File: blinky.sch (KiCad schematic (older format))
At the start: 38 parts, among them J1 MIC_CLK, J10 DEBUG, J11 SWD, J12 BATTERY, J13 UART, J14 5V, J15 3V3, J2 MIC_DOUT, J3 LED_DIN, J4 ACCEL_MISO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

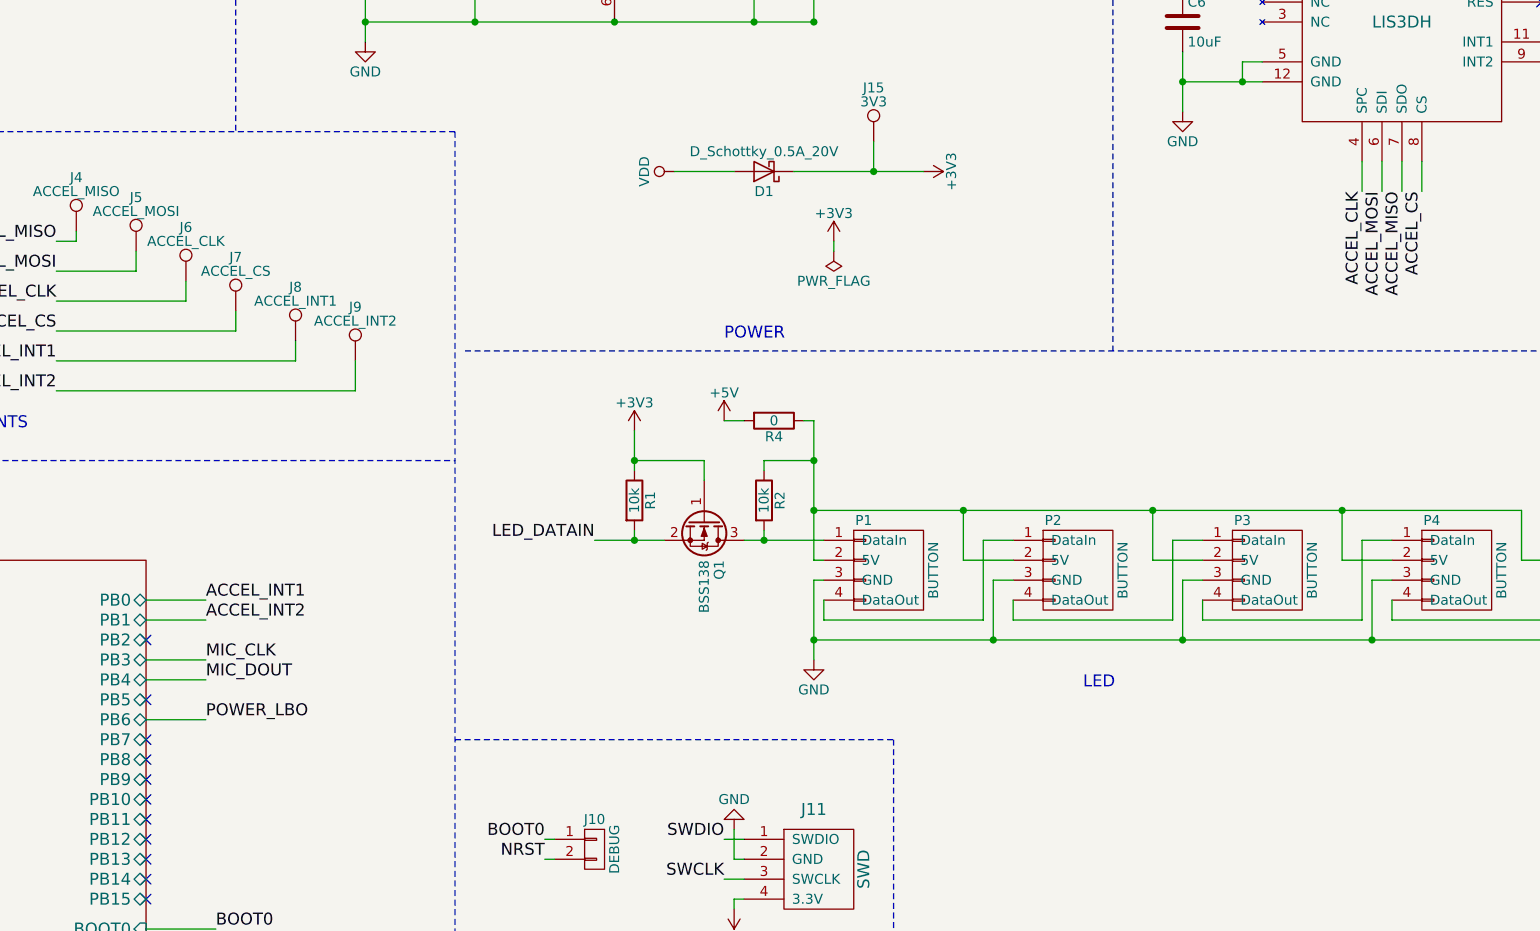
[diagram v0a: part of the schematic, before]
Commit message: Add heartbeat led
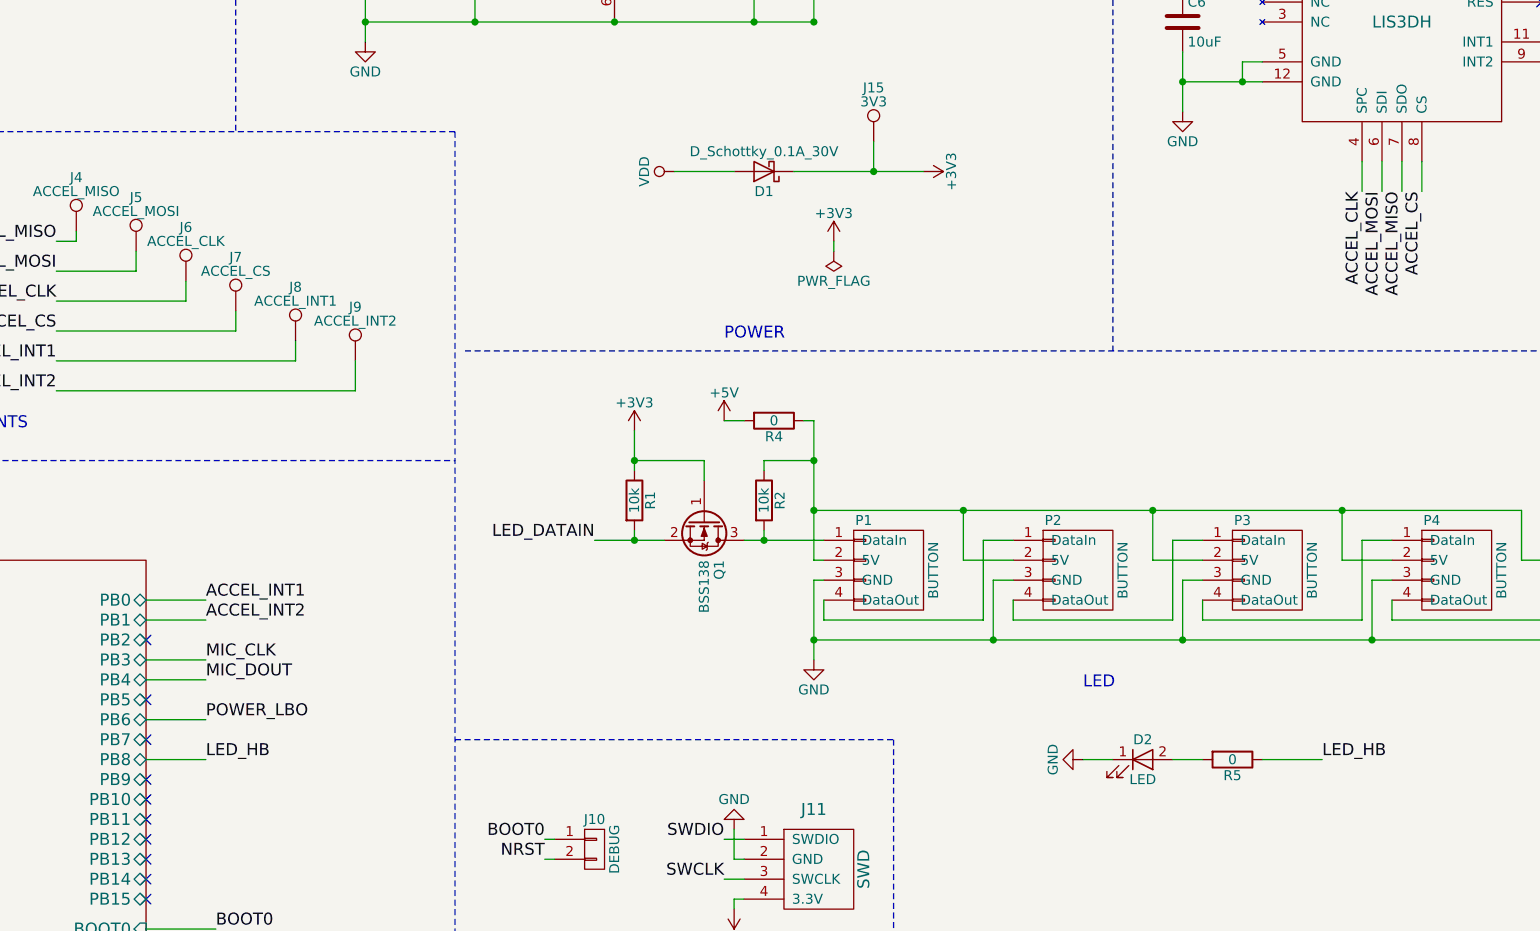
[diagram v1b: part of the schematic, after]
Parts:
- added D2: LED, Diodes_SMD:D_0603, symbol LED
- added R5: 0, Resistors_SMD:R_0603, symbol R
- D1: value D_Schottky_0.5A_20V -> D_Schottky_0.1A_30V; footprint Diodes_SMD:SOD-523 -> Diodes_SMD:D_0603; MFR Nexperia -> Comchip Technology; MPN PMEG2005EB,115 -> CDBU0130L; PN PMEG2005EB,115 -> (none); SPN 771-PMEG2005EBT/R -> 750-CDBU0130L
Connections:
- net GND: now also D2.1 (K)
- new net: D2.2 (A), R5.2
- new net LED_HB: R5.1
- no-connect marks 24 -> 23
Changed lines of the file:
@@
 EESchema Schematic File Version 2
-LIBS:blinky-rescue
 LIBS:power
 LIBS:device
@@
 $EndSheet
 $Comp
-L GND #PWR01
+L GND #PWR19
 U 1 1 59735157
 P 8250 2650
-F 0 "#PWR01" H 8250 2400 50  0001 C CNN
+F 0 "#PWR19" H 8250 2400 50  0001 C CNN
 F 1 "GND" H 8250 2500 50  0000 C CNN
 F 2 "" H 8250 2650 50  0001 C CNN
@@
 $EndComp
 $Comp
-L GND #PWR02
+L GND #PWR21
 U 1 1 59735414
 P 8450 1250
-F 0 "#PWR02" H 8450 1000 50  0001 C CNN
+F 0 "#PWR21" H 8450 1000 50  0001 C CNN
 F 1 "GND" H 8450 1100 50  0000 C CNN
 F 2 "" H 8450 1250 50  0001 C CNN
@@
 $EndComp
 $Comp
-L +5V #PWR03
+L +5V #PWR8
 U 1 1 59735989
 P 5950 4200
-F 0 "#PWR03" H 5950 4050 50  0001 C CNN
+F 0 "#PWR8" H 5950 4050 50  0001 C CNN
 F 1 "+5V" H 5950 4340 50  0000 C CNN
 F 2 "" H 5950 4200 50  0001 C CNN
@@
 $EndComp
 $Comp
-L GND #PWR04
+L GND #PWR13
 U 1 1 597359AA
 P 6400 5400
-F 0 "#PWR04" H 6400 5150 50  0001 C CNN
+F 0 "#PWR13" H 6400 5150 50  0001 C CNN
 F 1 "GND" H 6400 5250 50  0000 C CNN
 F 2 "" H 6400 5400 50  0001 C CNN
@@
 $EndComp
 $Comp
-L GND #PWR05
+L GND #PWR9
 U 1 1 59736818
 P 6000 6250
-F 0 "#PWR05" H 6000 6000 50  0001 C CNN
+F 0 "#PWR9" H 6000 6000 50  0001 C CNN
 F 1 "GND" H 6000 6100 50  0000 C CNN
 F 2 "" H 6000 6250 50  0001 C CNN
@@
 $EndComp
 $Comp
-L VDD #PWR06
+L VDD #PWR3
 U 1 1 5974FA3E
 P 4150 1000
-F 0 "#PWR06" H 4150 850 50  0001 C CNN
+F 0 "#PWR3" H 4150 850 50  0001 C CNN
 F 1 "VDD" H 4150 1150 50  0000 C CNN
 F 2 "" H 4150 1000 50  0001 C CNN
@@
 $EndComp
 $Comp
-L GND #PWR07
+L GND #PWR4
 U 1 1 5974FA44
 P 4150 2300
-F 0 "#PWR07" H 4150 2050 50  0001 C CNN
+F 0 "#PWR4" H 4150 2050 50  0001 C CNN
 F 1 "GND" H 4150 2150 50  0000 C CNN
 F 2 "" H 4150 2300 50  0001 C CNN
@@
 $EndComp
 $Comp
-L +5V #PWR08
+L +5V #PWR15
 U 1 1 5974FA78
 P 6750 1000
-F 0 "#PWR08" H 6750 850 50  0001 C CNN
+F 0 "#PWR15" H 6750 850 50  0001 C CNN
 F 1 "+5V" H 6750 1140 50  0000 C CNN
 F 2 "" H 6750 1000 50  0001 C CNN
@@
 $EndComp
 $Comp
-L +3V3 #PWR09
+L +3V3 #PWR16
 U 1 1 5974FA92
 P 6950 2950
-F 0 "#PWR09" H 6950 2800 50  0001 C CNN
+F 0 "#PWR16" H 6950 2800 50  0001 C CNN
 F 1 "+3V3" H 6950 3090 50  0000 C CNN
 F 2 "" H 6950 2950 50  0001 C CNN
@@
 P 6150 2950
 F 0 "D1" H 6150 3050 50  0000 C CNN
-F 1 "D_Schottky_0.5A_20V" H 6150 2850 50  0000 C CNN
-F 2 "Diodes_SMD:SOD-523" H 6150 2950 50  0001 C CNN
+F 1 "D_Schottky_0.1A_30V" H 6150 2850 50  0000 C CNN
+F 2 "Diodes_SMD:D_0603" H 6150 2950 50  0001 C CNN
 F 3 "" H 6150 2950 50  0001 C CNN
-F 4 "PMEG2005EB,115" H 6150 2950 60  0001 C CNN "PN"
-F 5 "Nexperia" H -1200 1750 50  0001 C CNN "MFR"
-F 6 "PMEG2005EB,115" H -1200 1750 50  0001 C CNN "MPN"
-F 7 "Mouser" H -1200 1750 50  0001 C CNN "SPR"
-F 8 "771-PMEG2005EBT/R" H -1200 1750 50  0001 C CNN "SPN"
-F 9 "" H -1200 1750 50  0001 C CNN "SPURL"
+F 4 "Comchip Technology" H -1200 1750 50  0001 C CNN "MFR"
+F 5 "CDBU0130L" H -1200 1750 50  0001 C CNN "MPN"
+F 6 "Mouser" H -1200 1750 50  0001 C CNN "SPR"
+F 7 "750-CDBU0130L" H -1200 1750 50  0001 C CNN "SPN"
 	1    6150 2950
 	-1   0    0    1
 $EndComp
 $Comp
-L +3V3 #PWR010
+L +3V3 #PWR18
 U 1 1 5974FC09
 P 8250 1900
-F 0 "#PWR010" H 8250 1750 50  0001 C CNN
+F 0 "#PWR18" H 8250 1750 50  0001 C CNN
 F 1 "+3V3" H 8250 2040 50  0000 C CNN
 F 2 "" H 8250 1900 50  0001 C CNN
@@
 $EndComp
 $Comp
-L +3V3 #PWR011
+L +3V3 #PWR20
 U 1 1 5974FD08
 P 8450 800
-F 0 "#PWR011" H 8450 650 50  0001 C CNN
+F 0 "#PWR20" H 8450 650 50  0001 C CNN
 F 1 "+3V3" H 8450 940 50  0000 C CNN
 F 2 "" H 8450 800 50  0001 C CNN
@@
 $EndComp
 $Comp
-L +3V3 #PWR012
+L +3V3 #PWR6
 U 1 1 5974FDE2
 P 5500 4250
-F 0 "#PWR012" H 5500 4100 50  0001 C CNN
+F 0 "#PWR6" H 5500 4100 50  0001 C CNN
 F 1 "+3V3" H 5500 4390 50  0000 C CNN
 F 2 "" H 5500 4250 50  0001 C CNN
@@
 $EndComp
 $Comp
-L +3V3 #PWR013
+L +3V3 #PWR10
 U 1 1 5974FF6A
 P 6000 6650
-F 0 "#PWR013" H 6000 6500 50  0001 C CNN
+F 0 "#PWR10" H 6000 6500 50  0001 C CNN
 F 1 "+3V3" H 6000 6790 50  0000 C CNN
 F 2 "" H 6000 6650 50  0001 C CNN
@@
 $EndComp
 $Comp
-L +3V3 #PWR014
+L +3V3 #PWR1
 U 1 1 59757575
 P 800 1150
-F 0 "#PWR014" H 800 1000 50  0001 C CNN
+F 0 "#PWR1" H 800 1000 50  0001 C CNN
 F 1 "+3V3" H 800 1290 50  0000 C CNN
 F 2 "" H 800 1150 50  0001 C CNN
@@
 $EndComp
 $Comp
-L GND #PWR015
+L GND #PWR2
 U 1 1 59757983
 P 800 2000
-F 0 "#PWR015" H 800 1750 50  0001 C CNN
+F 0 "#PWR2" H 800 1750 50  0001 C CNN
 F 1 "GND" H 800 1850 50  0000 C CNN
 F 2 "" H 800 2000 50  0001 C CNN
@@
 $EndComp
 $Comp
-L VDD #PWR016
+L VDD #PWR12
 U 1 1 597763DE
 P 6300 7200
-F 0 "#PWR016" H 6300 7050 50  0001 C CNN
+F 0 "#PWR12" H 6300 7050 50  0001 C CNN
 F 1 "VDD" H 6300 7350 50  0000 C CNN
 F 2 "" H 6300 7200 50  0001 C CNN
@@
 $EndComp
 $Comp
-L GND #PWR017
+L GND #PWR11
 U 1 1 59776525
 P 6250 7350
-F 0 "#PWR017" H 6250 7100 50  0001 C CNN
+F 0 "#PWR11" H 6250 7100 50  0001 C CNN
 F 1 "GND" H 6250 7200 50  0000 C CNN
 F 2 "" H 6250 7350 50  0001 C CNN
@@
 $EndComp
 $Comp
-L PWR_FLAG #FLG018
+L PWR_FLAG #FLG1
 U 1 1 59776D41
 P 6250 7250
-F 0 "#FLG018" H 6250 7325 50  0001 C CNN
+F 0 "#FLG1" H 6250 7325 50  0001 C CNN
 F 1 "PWR_FLAG" H 6250 7400 50  0000 C CNN
 F 2 "" H 6250 7250 50  0001 C CNN
@@
 $EndComp
 $Comp
-L +3V3 #PWR019
+L +3V3 #PWR14
 U 1 1 5977B020
 P 6500 3300
-F 0 "#PWR019" H 6500 3150 50  0001 C CNN
+F 0 "#PWR14" H 6500 3150 50  0001 C CNN
 F 1 "+3V3" H 6500 3440 50  0000 C CNN
 F 2 "" H 6500 3300 50  0001 C CNN
@@
 $EndComp
 $Comp
-L PWR_FLAG #FLG020
+L PWR_FLAG #FLG2
 U 1 1 5977B2DF
 P 6500 3350
-F 0 "#FLG020" H 6500 3425 50  0001 C CNN
+F 0 "#FLG2" H 6500 3425 50  0001 C CNN
 F 1 "PWR_FLAG" H 6500 3500 50  0000 C CNN
 F 2 "" H 6500 3350 50  0001 C CNN
@@
 NoConn ~ 3050 6100
 NoConn ~ 3050 6000
-NoConn ~ 3050 5900
 NoConn ~ 3050 5800
 NoConn ~ 3050 5600
@@
 	5100 7250 5150 7250
 $Comp
-L GND #PWR021
+L GND #PWR5
 U 1 1 59DAA5B4
 P 5100 7100
-F 0 "#PWR021" H 5100 6850 50  0001 C CNN
+F 0 "#PWR5" H 5100 6850 50  0001 C CNN
 F 1 "GND" H 5100 6950 50  0000 C CNN
 F 2 "" H 5100 7100 50  0001 C CNN
@@
 	6050 4200 5950 4200
 $Comp
-L VDD #PWR022
+L VDD #PWR7
 U 1 1 5A04A8BB
 P 5700 2950
-F 0 "#PWR022" H 5700 2800 50  0001 C CNN
+F 0 "#PWR7" H 5700 2800 50  0001 C CNN
 F 1 "VDD" H 5700 3100 50  0000 C CNN
 F 2 "" H 5700 2950 50  0001 C CNN
@@
 	6700 2800 6700 2950
 Connection ~ 6700 2950
+$Comp
+L LED D2
+U 1 1 5A1E07BE
+P 8050 5900
+F 0 "D2" H 8050 6000 50  0000 C CNN
+F 1 "LED" H 8050 5800 50  0000 C CNN
+F 2 "Diodes_SMD:D_0603" H 8050 5900 50  0001 C CNN
+F 3 "" H 8050 5900 50  0001 C CNN
+	1    8050 5900
+	1    0    0    -1
+$EndComp
+$Comp
+L R R5
+U 1 1 5A1E0EDE
+P 8500 5900
+F 0 "R5" V 8580 5900 50  0000 C CNN
+F 1 "0" V 8500 5900 50  0000 C CNN
+F 2 "Resistors_SMD:R_0603" V 8430 5900 50  0001 C CNN
+F 3 "" H 8500 5900 50  0001 C CNN
+F 4 "YAGEO" H 3000 1300 50  0001 C CNN "MFR"
+F 5 "RC0603JR-070RL" H 3000 1300 50  0001 C CNN "MPN"
+F 6 "Mouser" H 3000 1300 50  0001 C CNN "SPR"
+F 7 "603-RC0603JR-070RL" H 3000 1300 50  0001 C CNN "SPN"
+	1    8500 5900
+	0    1    1    0
+$EndComp
+$Comp
+L GND #PWR17
+U 1 1 5A1E106E
+P 7750 5900
+F 0 "#PWR17" H 7750 5650 50  0001 C CNN
+F 1 "GND" H 7750 5750 50  0000 C CNN
+F 2 "" H 7750 5900 50  0001 C CNN
+F 3 "" H 7750 5900 50  0001 C CNN
+	1    7750 5900
+	0    1    1    0
+$EndComp
+Wire Wire Line
+	8350 5900 8200 5900
+Wire Wire Line
+	7900 5900 7750 5900
+Text Label 3350 5900 0    60   ~ 0
+LED_HB
+Wire Wire Line
+	3050 5900 3350 5900
+Text Label 8950 5900 0    60   ~ 0
+LED_HB
+Wire Wire Line
+	8950 5900 8650 5900
 $EndSCHEMATC
